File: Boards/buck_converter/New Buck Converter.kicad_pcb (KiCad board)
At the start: 2 copper layers, 50.8 x 50.8 mm, 25 parts, among them J1 Conn_01x02_Female, J2 Conn_01x02_Female, U1 TPS560430YF

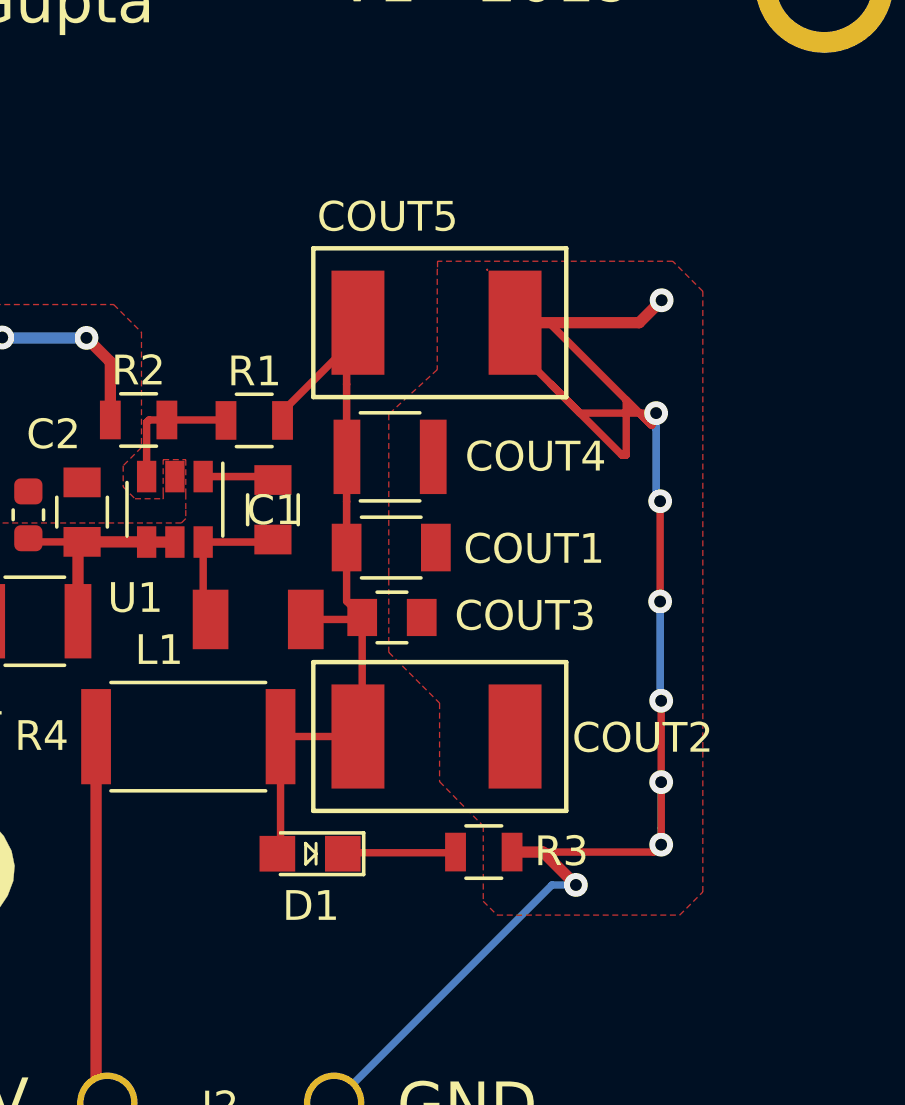
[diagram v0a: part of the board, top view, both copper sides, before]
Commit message: Pushing Buck Converter REV_2
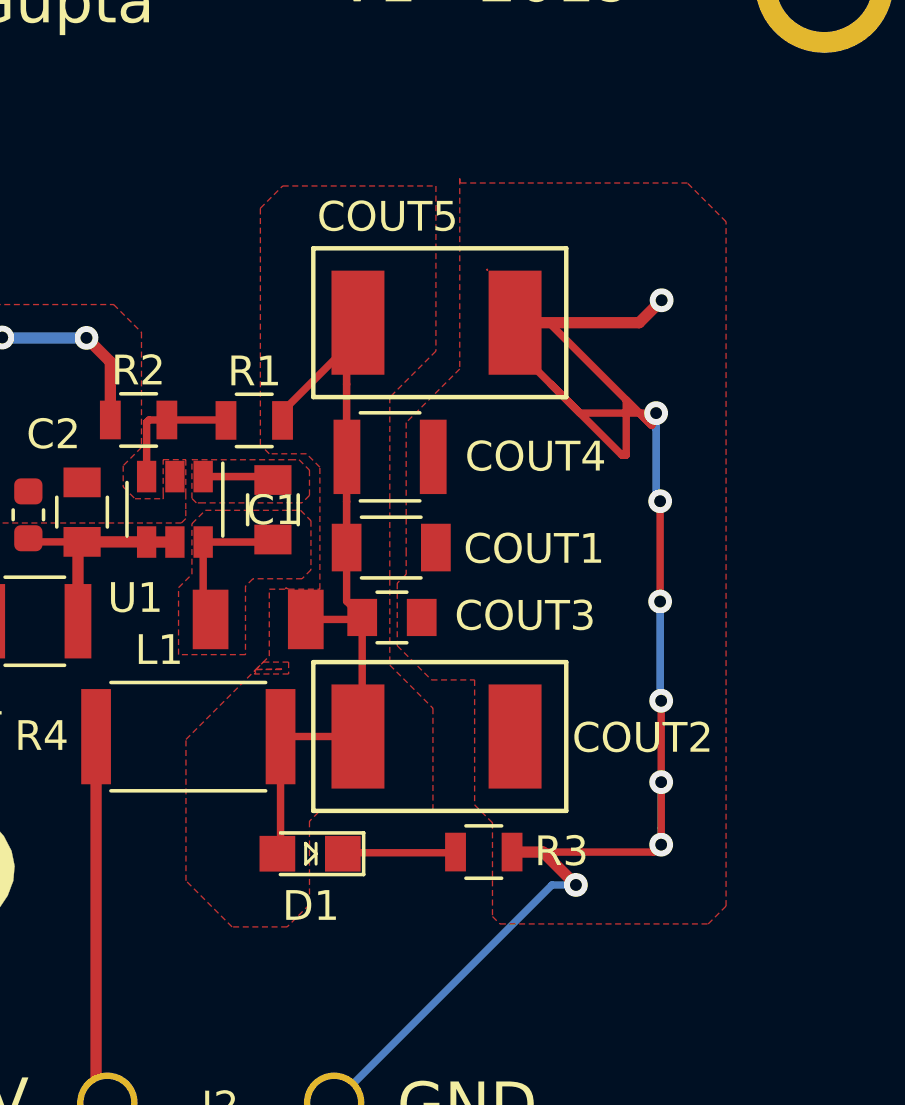
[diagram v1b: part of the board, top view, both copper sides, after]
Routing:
- added copper zone on F.Cu, net Net-(C1-Pad1)
- added copper zone on F.Cu, net Net-(C1-Pad2)
- added copper zone on F.Cu, net Net-(COUT1-Pad1)
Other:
- net class Default: clearance 0.2 -> 0.1524; trace_width 0.25 -> 0.1524; via_dia 0.8 -> 0.6096; via_drill 0.4 -> 0.3048
- rule trace_clearance: 0.2 -> 0.1524
- rule trace_min: 0.0254 -> 0.1524
- rule via_min_drill: 0.3 -> 0.3048
- rule via_min_size: 0.4 -> 0.1524
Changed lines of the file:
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@@
   (page A4)
   (layers
-    (0 F.Cu signal hide)
-    (31 B.Cu signal)
+    (0 F.Cu signal)
+    (31 B.Cu signal hide)
     (32 B.Adhes user)
     (33 F.Adhes user)
@@
   )
   (setup
-    (last_trace_width 0.25)
+    (last_trace_width 0.1524)
     (user_trace_width 0.254)
     (user_trace_width 0.381)
-    (trace_clearance 0.2)
+    (trace_clearance 0.1524)
     (zone_clearance 0.1524)
     (zone_45_only no)
-    (trace_min 0.0254)
+    (trace_min 0.1524)
     (segment_width 0.2)
     (edge_width 0.15)
-    (via_size 0.8)
-    (via_drill 0.4)
-    (via_min_size 0.4)
-    (via_min_drill 0.3)
+    (via_size 0.6096)
+    (via_drill 0.3048)
+    (via_min_size 0.1524)
+    (via_min_drill 0.3048)
     (uvia_size 0.3)
     (uvia_drill 0.1)
@@
       (outputformat 1)
       (mirror false)
-      (drillshape 1)
+      (drillshape 0)
       (scaleselection 1)
-      (outputdirectory ""))
+      (outputdirectory "2_11_2019/"))
   )
   (net 0 "")
@@
   (net 9 "Net-(D1-Pad1)")
   (net_class Default "This is the default net class."
-    (clearance 0.2)
-    (trace_width 0.25)
-    (via_dia 0.8)
-    (via_drill 0.4)
+    (clearance 0.1524)
+    (trace_width 0.1524)
+    (via_dia 0.6096)
+    (via_drill 0.3048)
     (uvia_dia 0.3)
     (uvia_drill 0.1)
@@
     (polygon
       (pts
-        (xy 135.49376 93.89872) (xy 135.49376 97.27438) (xy 134.51332 98.171) (xy 133.86562 98.77044) (xy 133.86562 104.0003)
-        (xy 133.86562 106.77144) (xy 134.99338 107.8992) (xy 135.5725 108.47832) (xy 135.5725 111.11738) (xy 136.4742 112.0394)
-        (xy 137.04062 112.60582) (xy 137.04062 115.1382) (xy 137.50544 115.60302) (xy 143.64208 115.60302) (xy 144.41932 114.82578)
-        (xy 144.41932 94.6404) (xy 143.4084 93.62948) (xy 135.50392 93.62948) (xy 135.50392 93.88856)
-      )
-    )
-  )
-  (zone (net 4) (net_name GND) (layer F.Cu) (hatch edge 0.508)
-    (connect_pads yes (clearance 0.1524))
-    (min_thickness 0.1524)
-    (fill yes (arc_segments 16) (thermal_gap 0.508) (thermal_bridge_width 0.508))
-    (polygon
-      (pts
         (xy 126.28372 101.43236) (xy 126.28372 100.29698) (xy 127.04318 100.29698) (xy 127.04318 101.4349) (xy 127.04318 101.9937)
         (xy 127.04318 102.27818) (xy 126.89586 102.4255) (xy 120.015 102.4255) (xy 118.6561 103.7844) (xy 113.57864 103.7844)
@@
       )
     )
+  )
+  (zone (net 4) (net_name GND) (layer F.Cu) (hatch edge 0.508)
+    (connect_pads yes (clearance 0.1524))
+    (min_thickness 0.1524)
+    (fill yes (arc_segments 16) (thermal_gap 0.508) (thermal_bridge_width 0.508))
+    (polygon
+      (pts
+        (xy 136.25 90.85) (xy 136.25 97.25) (xy 134.45 99.05) (xy 134.45 103.35) (xy 134.45 104.15)
+        (xy 134.15 104.45) (xy 134.15 106.55) (xy 135.3 107.7) (xy 136.75 107.7) (xy 136.75 111.9)
+        (xy 137.35 112.5) (xy 137.35 115.65) (xy 137.6 115.9) (xy 144.6 115.9) (xy 145.2 115.3)
+        (xy 145.2 92.3) (xy 143.9 91) (xy 136.25 91)
+      )
+    )
+  )
+  (zone (net 2) (net_name "Net-(C1-Pad1)") (layer F.Cu) (hatch edge 0.508)
+    (connect_pads yes (clearance 0.1524))
+    (min_thickness 0.1524)
+    (fill yes (arc_segments 16) (thermal_gap 0.508) (thermal_bridge_width 0.508))
+    (polygon
+      (pts
+        (xy 131.25 102.35) (xy 131.25 104) (xy 130.95 104.3) (xy 129.3 104.3) (xy 129.05 104.55)
+        (xy 129.05 106.85) (xy 126.8 106.85) (xy 126.8 104.6) (xy 127.25 104.15) (xy 127.25 102.45)
+        (xy 127.7 102) (xy 130.9 102)
+      )
+    )
+  )
+  (zone (net 8) (net_name "Net-(COUT1-Pad1)") (layer F.Cu) (hatch edge 0.508)
+    (connect_pads yes (clearance 0.1524))
+    (min_thickness 0.1524)
+    (fill yes (arc_segments 16) (thermal_gap 0.508) (thermal_bridge_width 0.508))
+    (polygon
+      (pts
+        (xy 135.45 96.65) (xy 133.9 98.2) (xy 133.9 107.2) (xy 135.35 108.65) (xy 135.35 112.15)
+        (xy 131.5 112.15) (xy 131.2 112.45) (xy 131.2 115.25) (xy 130.45 116) (xy 128.6 116)
+        (xy 127.05 114.45) (xy 127.05 109.7) (xy 129.4 107.35) (xy 130.25 107.35) (xy 130.270238 107.329762)
+        (xy 129.4 107.35) (xy 129.85 106.9) (xy 129.85 104.65) (xy 130.4 104.65) (xy 130.4 104.6)
+        (xy 130.5 104.65) (xy 131.55 104.65) (xy 131.55 100.55) (xy 131.1 100.1) (xy 129.85 100.1)
+        (xy 129.55 99.8) (xy 129.55 91.85) (xy 130.3 91.1) (xy 135.45 91.1)
+      )
+    )
+  )
+  (zone (net 8) (net_name "Net-(COUT1-Pad1)") (layer F.Cu) (hatch edge 0.508)
+    (connect_pads yes (clearance 0.1524))
+    (min_thickness 0.1524)
+    (fill yes (arc_segments 16) (thermal_gap 0.508) (thermal_bridge_width 0.508))
+    (polygon
+      (pts
+        (xy 129.35 107.4) (xy 129.65 107.1) (xy 130.5 107.1) (xy 130.5 107.5) (xy 129.35 107.5)
+        (xy 129.4 107.45)
+      )
+    )
+  )
+  (zone (net 1) (net_name "Net-(C1-Pad2)") (layer F.Cu) (hatch edge 0.508)
+    (connect_pads yes (clearance 0.1524))
+    (min_thickness 0.1524)
+    (fill yes (arc_segments 16) (thermal_gap 0.508) (thermal_bridge_width 0.508))
+    (polygon
+      (pts
+        (xy 127.25 100.3) (xy 130.55 100.3) (xy 130.85 100.3) (xy 131.2 100.65) (xy 131.2 101.5)
+        (xy 130.95 101.75) (xy 127.65 101.75) (xy 127.4 101.75) (xy 127.25 101.6)
+      )
+    )

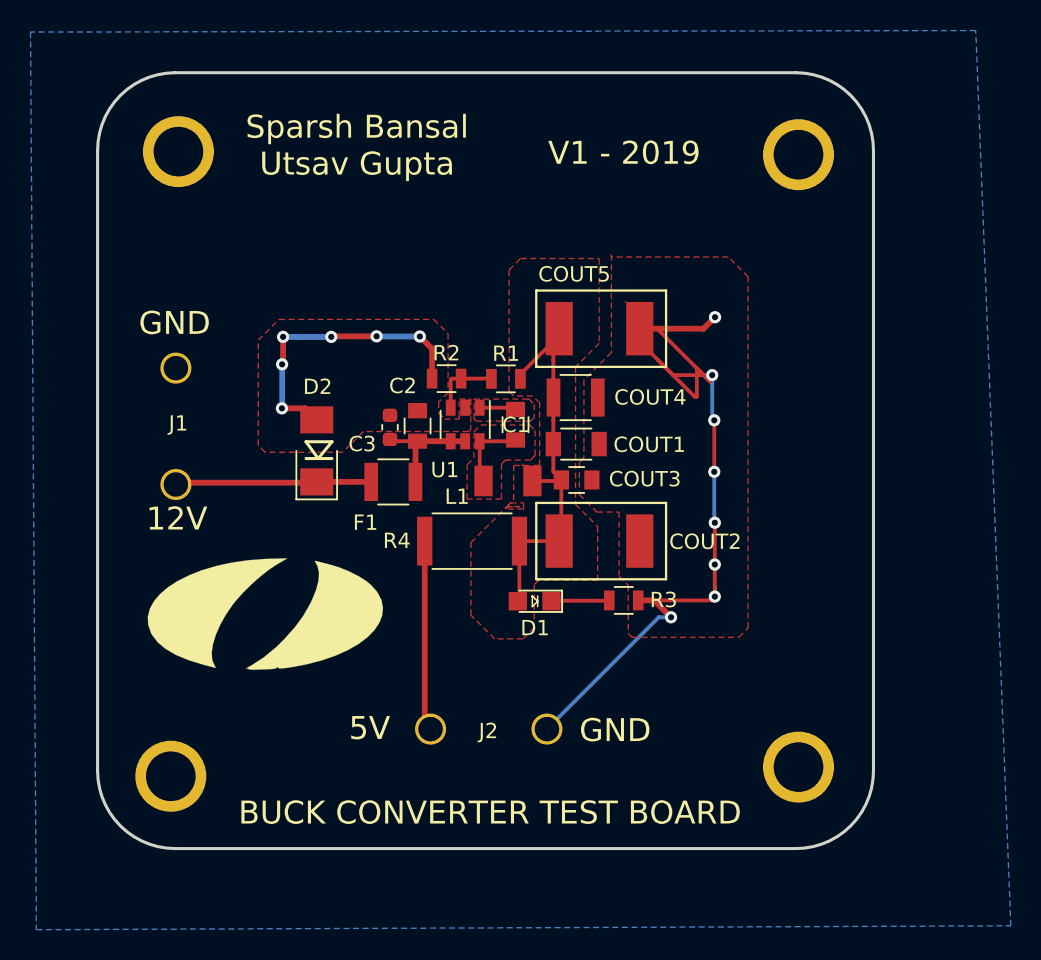
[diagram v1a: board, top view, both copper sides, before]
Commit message: Updated Buck Converter Schematic and the Layout for REV2
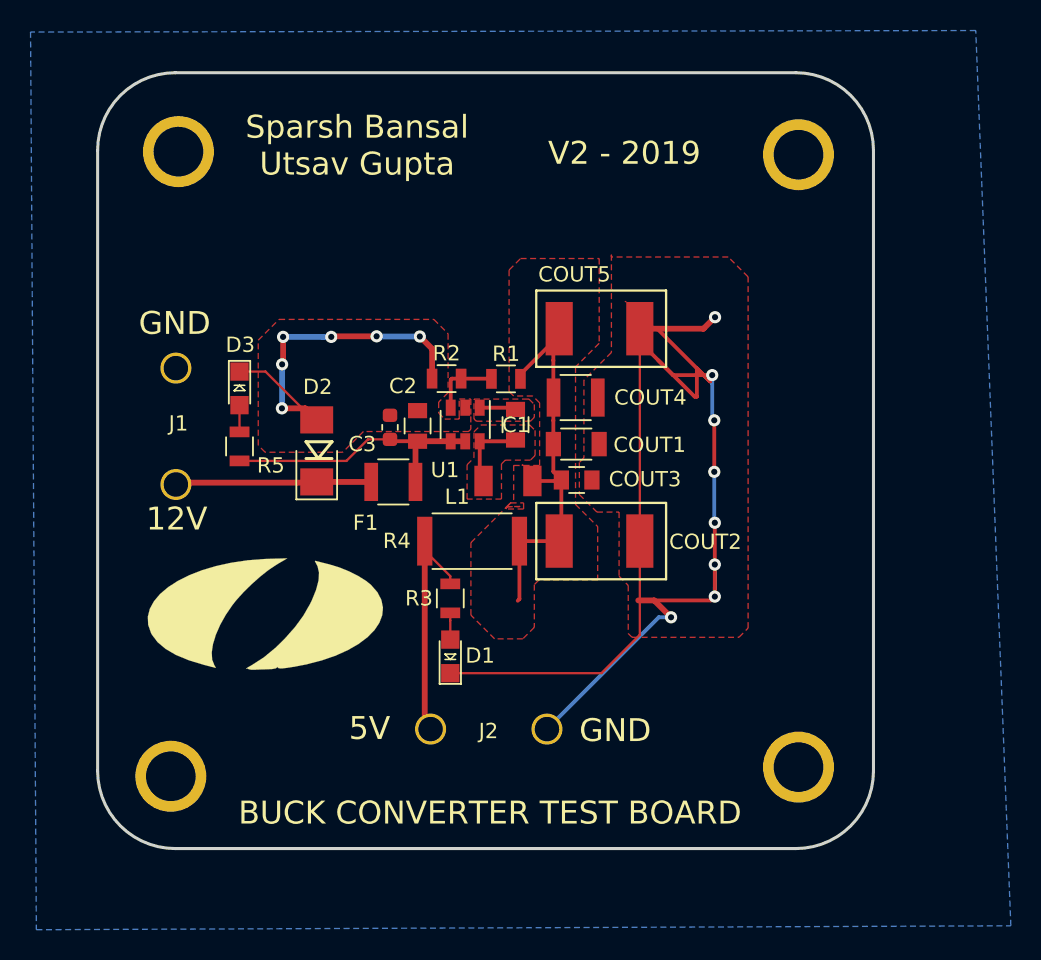
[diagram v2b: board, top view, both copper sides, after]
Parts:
- added D3: LED_0805, footprints:LED_0805_OEM, F.Cu at (111.9, 99.6)
- added R5: R_200, footprints:R_0805_OEM, F.Cu at (111.9, 103.4)
- moved R3 11.4 mm to (125.7, 113.3), turned to 270 degrees
- moved D1 6.60 mm to (125.7, 117.2), turned to 90 degrees
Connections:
- D1 pad 1: Net-(D1-Pad1) -> GND
- D1 pad 2: Net-(COUT1-Pad1) -> Net-(D1-Pad2)
- R3 pad 1: Net-(D1-Pad1) -> VCC
- R3 pad 2: GND -> Net-(D1-Pad2)
- R4 pad 2: /5V -> VCC
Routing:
- net GND: track 79.4 -> 119.3 mm
- net Net-(C2-Pad1): track 7.70 -> 18.1 mm
- net Net-(D1-Pad1): track 3.80 -> 0.00 mm
- net VCC: track 0.00 -> 2.27 mm
- net Net-(D3-Pad2): track 0.00 -> 1.75 mm
- net Net-(D1-Pad2): track 0.00 -> 1.75 mm
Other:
- board text added: "V2 - 2019"
- board text removed: "V1 - 2019"
